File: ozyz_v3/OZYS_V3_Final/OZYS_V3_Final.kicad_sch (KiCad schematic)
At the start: 26 parts, among them CN1 532610571, J1 5037630491, U1 ISO1044BD, U3 MKDV32GCL-STP, U4 STM32G474CETx, X2 MC-306 32.768kHz 6.0pF 20ppm

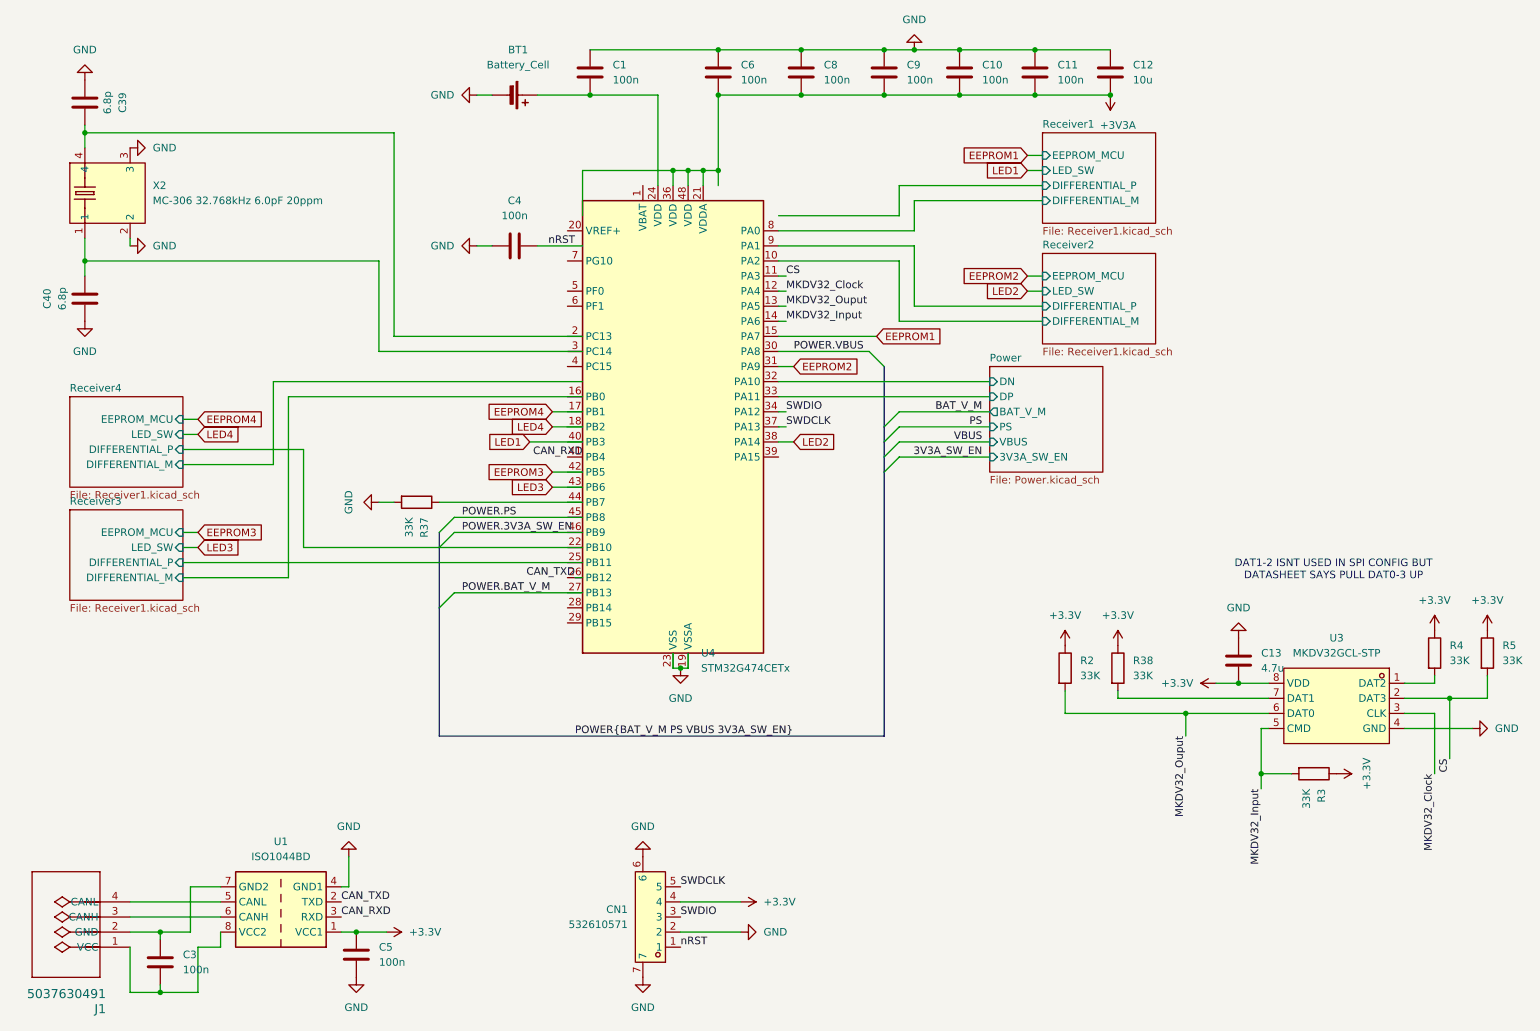
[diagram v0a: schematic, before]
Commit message: OZYS and EPSILON schematics updated.
OZYS
- New 3.5 PJ-320A-4P DIP
- Fixed TPS Regulator Connections
- Fixed STM32 Connections
- Added Associated .ioc for stm32 pin config
- Loading Capacitance of LSE based off  an5093 STM datasheet
EPSILON
- same 3.5 as OZYS
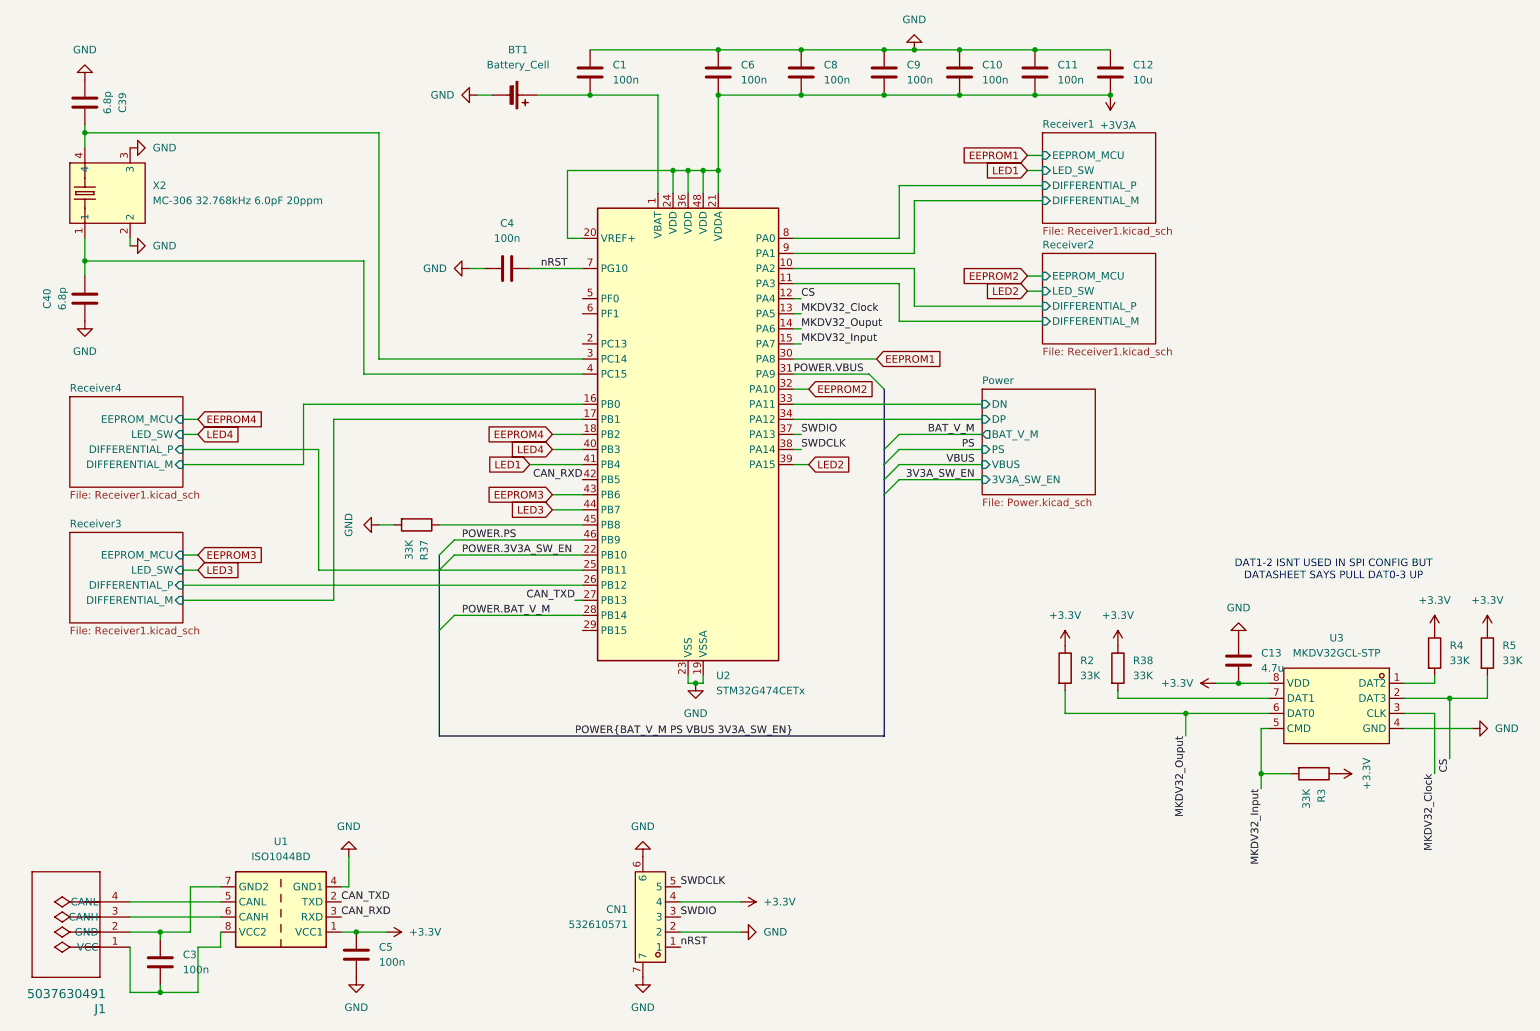
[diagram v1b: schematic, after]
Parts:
- removed U4: STM32G474CETx, Package_QFP:LQFP-48_7x7mm_P0.5mm, symbol MCU_ST_STM32G4:STM32G474CETx
- added U2: STM32G474CETx, Package_QFP:LQFP-48_7x7mm_P0.5mm, symbol MCU_ST_STM32G4:STM32G474CETx
- BT1: footprint (none) -> Rocketry_Manual:SEIKO_ML414H_IV01E
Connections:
- net +3V3A: now also U2.20 (VREF+), U2.21 (VDDA), U2.24 (VDD), U2.36 (VDD), U2.48 (VDD)
- net CAN_RXD: now also U2.42 (PB5)
- net CAN_TXD: now also U2.27 (PB13)
- net CS: now also U2.12 (PA4)
- net EEPROM1: now also U2.30 (PA8)
- net EEPROM2: now also U2.32 (PA10)
- net EEPROM3: now also U2.43 (PB6)
- net EEPROM4: now also U2.18 (PB2)
- net GND: now also U2.19 (VSSA), U2.23 (VSS), U2.35 (VSS), U2.47 (VSS)
- net LED1: now also U2.41 (PB4)
- net LED2: now also U2.39 (PA15)
- net LED3: now also U2.44 (PB7)
- net LED4: now also U2.40 (PB3)
- net MKDV32_Clock: now also U2.13 (PA5)
- net MKDV32_Input: now also U2.15 (PA7)
- net MKDV32_Ouput: now also U2.14 (PA6)
- net POWER.3V3A_SW_EN: now also U2.22 (PB10)
- net POWER.BAT_V_M: now also U2.28 (PB14)
- net POWER.PS: now also U2.46 (PB9)
- net POWER.VBUS: now also U2.31 (PA9)
- net Power/DN: now also U2.33 (PA11)
- net Power/DP: now also U2.34 (PA12)
- net Receiver1/DIFFERENTIAL_M: now also U2.9 (PA1)
- net Receiver1/DIFFERENTIAL_P: now also U2.8 (PA0)
- net Receiver2/DIFFERENTIAL_M: now also U2.11 (PA3)
- net Receiver2/DIFFERENTIAL_P: now also U2.10 (PA2)
- net Receiver3/DIFFERENTIAL_M: now also U2.17 (PB1)
- net Receiver3/DIFFERENTIAL_P: now also U2.26 (PB12)
- net Receiver4/DIFFERENTIAL_M: now also U2.16 (PB0)
- net Receiver4/DIFFERENTIAL_P: now also U2.25 (PB11)
- net SWDCLK: now also U2.38 (PA14)
- net SWDIO: now also U2.37 (PA13)
- net nRST: now also U2.7 (PG10)
- net at BT1.1 (+), C1.2: now also U2.1 (VBAT)
- net at C40.2, X2.1: now also U2.4 (PC15)
- net at C39.2, X2.4: now also U2.3 (PC14)
- net at R37.1: now also U2.45 (PB8)
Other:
- moved on the sheet: C4, R37
